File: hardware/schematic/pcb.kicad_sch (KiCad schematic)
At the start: 10 parts, among them J1 L, J2 R, J3 IR, J4 R n20 motor, J5 L n20 motor, J6 OLED, J7 L DRIVE, J8 R DRIVE, SW1 SW_DPST_x2

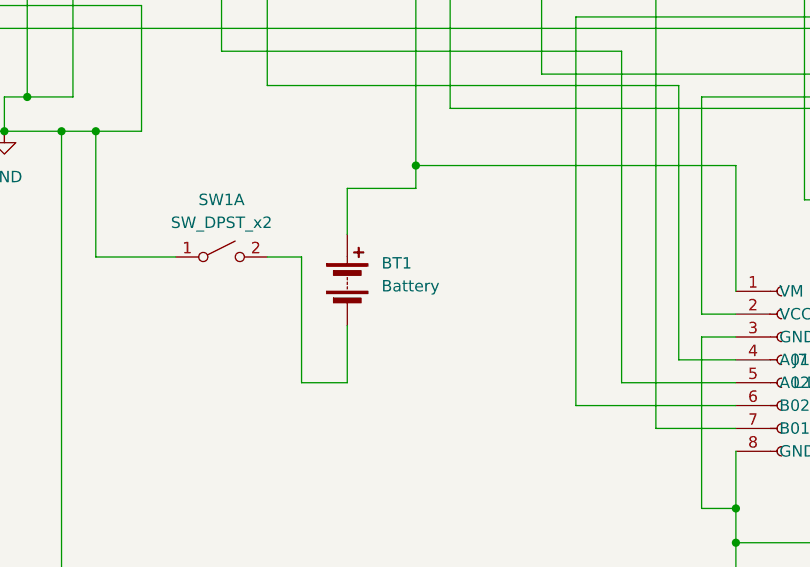
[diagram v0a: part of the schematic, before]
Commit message: Hardware: Minor schematic changes
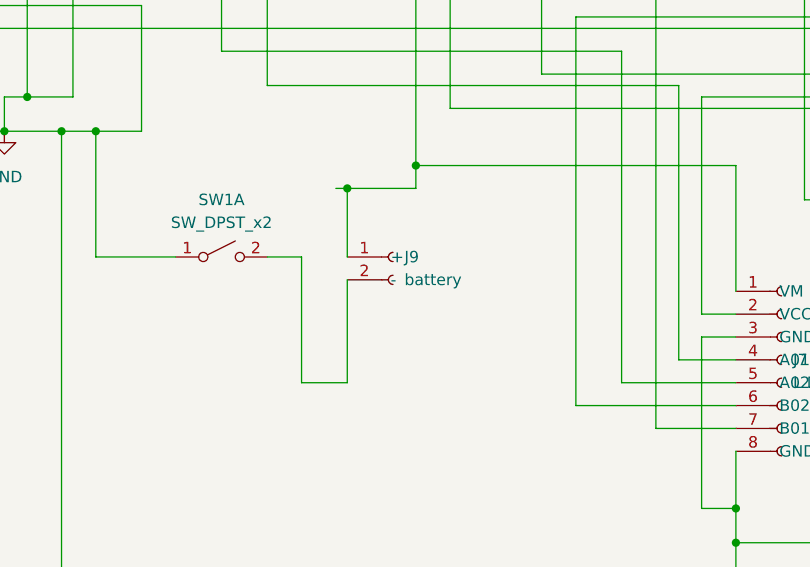
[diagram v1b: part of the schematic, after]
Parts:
- removed BT1: Battery, symbol Device:Battery
- added J9: battery, symbol Connector:Conn_01x02_Socket
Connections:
- net at SW1.2 (B): now also J9.2 (-)
- net at J1.15 (VIN), J7.1 (VM): now also J9.1 (+)
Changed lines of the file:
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@@
+	)
+	(junction
+		(at 81.28 139.7)
+		(diameter 0)
+		(color 0 0 0 0)
 	)
 	(junction
@@
 	(wire
 		(pts
+			(xy 81.28 149.86) (xy 81.28 161.29)
+		)
+		(stroke
+			(width 0)
+			(type default)
+		)
+	)
+	(wire
+		(pts
 			(xy 245.11 130.81) (xy 245.11 119.38)
 		)
@@
 	(wire
 		(pts
-			(xy 81.28 161.29) (xy 81.28 154.94)
-		)
-		(stroke
-			(width 0)
-			(type default)
-		)
-	)
-	(wire
-		(pts
 			(xy 72.39 80.01) (xy 72.39 128.27)
 		)
@@
 	(wire
 		(pts
+			(xy 80.01 139.7) (xy 81.28 139.7)
+		)
+		(stroke
+			(width 0)
+			(type default)
+		)
+	)
+	(wire
+		(pts
 			(xy 50.8 85.09) (xy 50.8 129.54)
 		)
@@
 	(wire
 		(pts
+			(xy 81.28 139.7) (xy 81.28 147.32)
+		)
+		(stroke
+			(width 0)
+			(type default)
+		)
+	)
+	(wire
+		(pts
 			(xy 167.64 35.56) (xy 167.64 38.1)
 		)
@@
 		(pts
 			(xy 111.76 49.53) (xy 111.76 80.01)
-		)
-		(stroke
-			(width 0)
-			(type default)
-		)
-	)
-	(wire
-		(pts
-			(xy 81.28 139.7) (xy 81.28 144.78)
 		)
 		(stroke
@@
 	)
 	(symbol
-		(lib_id "Device:Battery")
-		(at 81.28 149.86 0)
-		(unit 1)
-		(exclude_from_sim no)
-		(in_bom yes)
-		(on_board yes)
-		(dnp no)
-		(fields_autoplaced yes)
-		(property "Reference" "BT1"
-			(at 85.09 148.0184 0)
-			(effects
-				(font
-					(size 1.27 1.27)
-				)
-				(justify left)
-			)
-		)
-		(property "Value" "Battery"
-			(at 85.09 150.5584 0)
-			(effects
-				(font
-					(size 1.27 1.27)
-				)
-				(justify left)
-			)
-		)
-		(property "Footprint" ""
-			(at 81.28 148.336 90)
-			(effects
-				(font
-					(size 1.27 1.27)
-				)
-				(hide yes)
-			)
-		)
-		(property "Datasheet" "~"
-			(at 81.28 148.336 90)
-			(effects
-				(font
-					(size 1.27 1.27)
-				)
-				(hide yes)
-			)
-		)
-		(property "Description" "Multiple-cell battery"
-			(at 81.28 149.86 0)
-			(effects
-				(font
-					(size 1.27 1.27)
-				)
-				(hide yes)
-			)
-		)
-		(property "Sim.Device" "V"
-			(at 81.28 149.86 0)
-			(effects
-				(font
-					(size 1.27 1.27)
-				)
-				(hide yes)
-			)
-		)
-		(property "Sim.Type" "DC"
-			(at 81.28 149.86 0)
-			(effects
-				(font
-					(size 1.27 1.27)
-				)
-				(hide yes)
-			)
-		)
-		(property "Sim.Pins" "1=+ 2=-"
-			(at 81.28 149.86 0)
-			(effects
-				(font
-					(size 1.27 1.27)
-				)
-				(hide yes)
-			)
-		)
-		(pin "2"
-		)
-		(pin "1"
-		)
-		(instances
-			(project ""
-				(path "/bf33ebff-7199-46c5-b9b5-ecab4d26825a"
-					(reference "BT1")
-					(unit 1)
-				)
-			)
-		)
-	)
-	(symbol
 		(lib_id "Connector:Conn_01x06_Socket")
 		(at 191.77 87.63 0)
@@
 					(unit 1)
 				)
+			)
+		)
+	)
+	(symbol
+		(lib_id "Connector:Conn_01x02_Socket")
+		(at 86.36 147.32 0)
+		(unit 1)
+		(exclude_from_sim no)
+		(in_bom yes)
+		(on_board yes)
+		(dnp no)
+		(property "Reference" "J9"
+			(at 87.63 147.3199 0)
+			(effects
+				(font
+					(size 1.27 1.27)
+				)
+				(justify left)
+			)
+		)
+		(property "Value" "battery"
+			(at 87.63 149.8599 0)
+			(effects
+				(font
+					(size 1.27 1.27)
+				)
+				(justify left)
+			)
+		)
+		(property "Footprint" ""
+			(at 86.36 147.32 0)
+			(effects
+				(font
+					(size 1.27 1.27)
+				)
+				(hide yes)
+			)
+		)
+		(property "Datasheet" "~"
+			(at 86.36 147.32 0)
+			(effects
+				(font
+					(size 1.27 1.27)
+				)
+				(hide yes)
+			)
+		)
+		(property "Description" "Generic connector, single row, 01x02, script generated"
+			(at 86.36 147.32 0)
+			(effects
+				(font
+					(size 1.27 1.27)
+				)
+				(hide yes)
+			)
+		)
+		(pin "1"
+		)
+		(pin "2"
+		)
+		(instances
+			(project ""
+				(path "/bf33ebff-7199-46c5-b9b5-ecab4d26825a"
+					(reference "J9")
+					(unit 1)
+				)

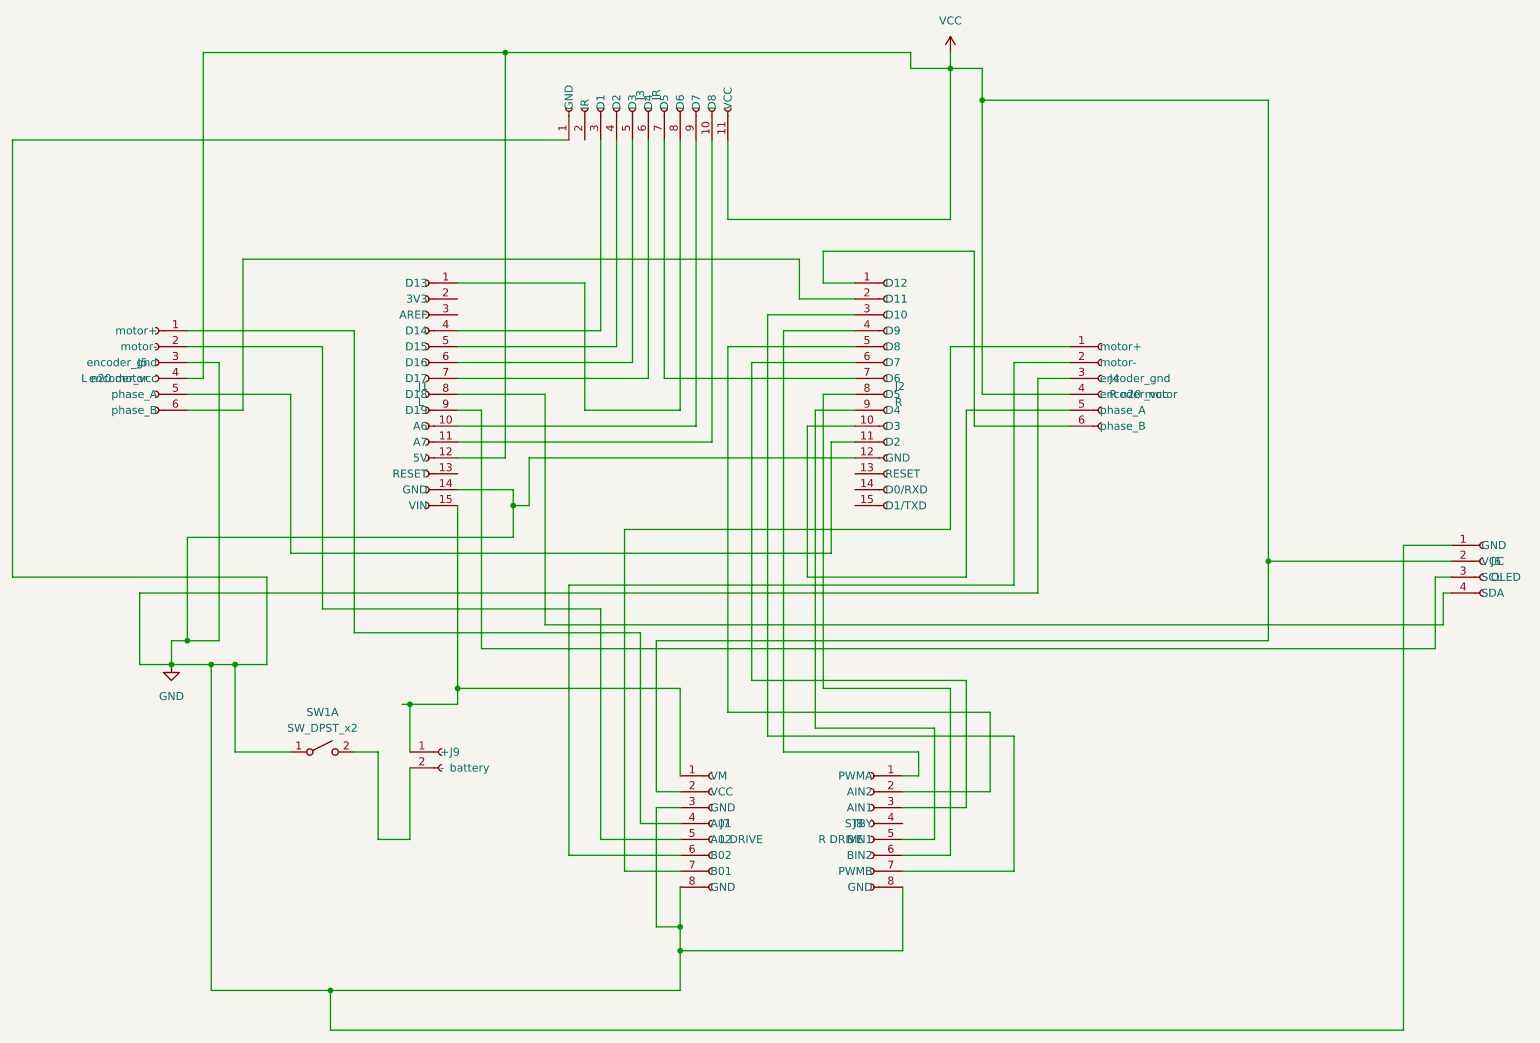
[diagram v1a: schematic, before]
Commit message: Hardware: Changed schematic according to new pin mapping
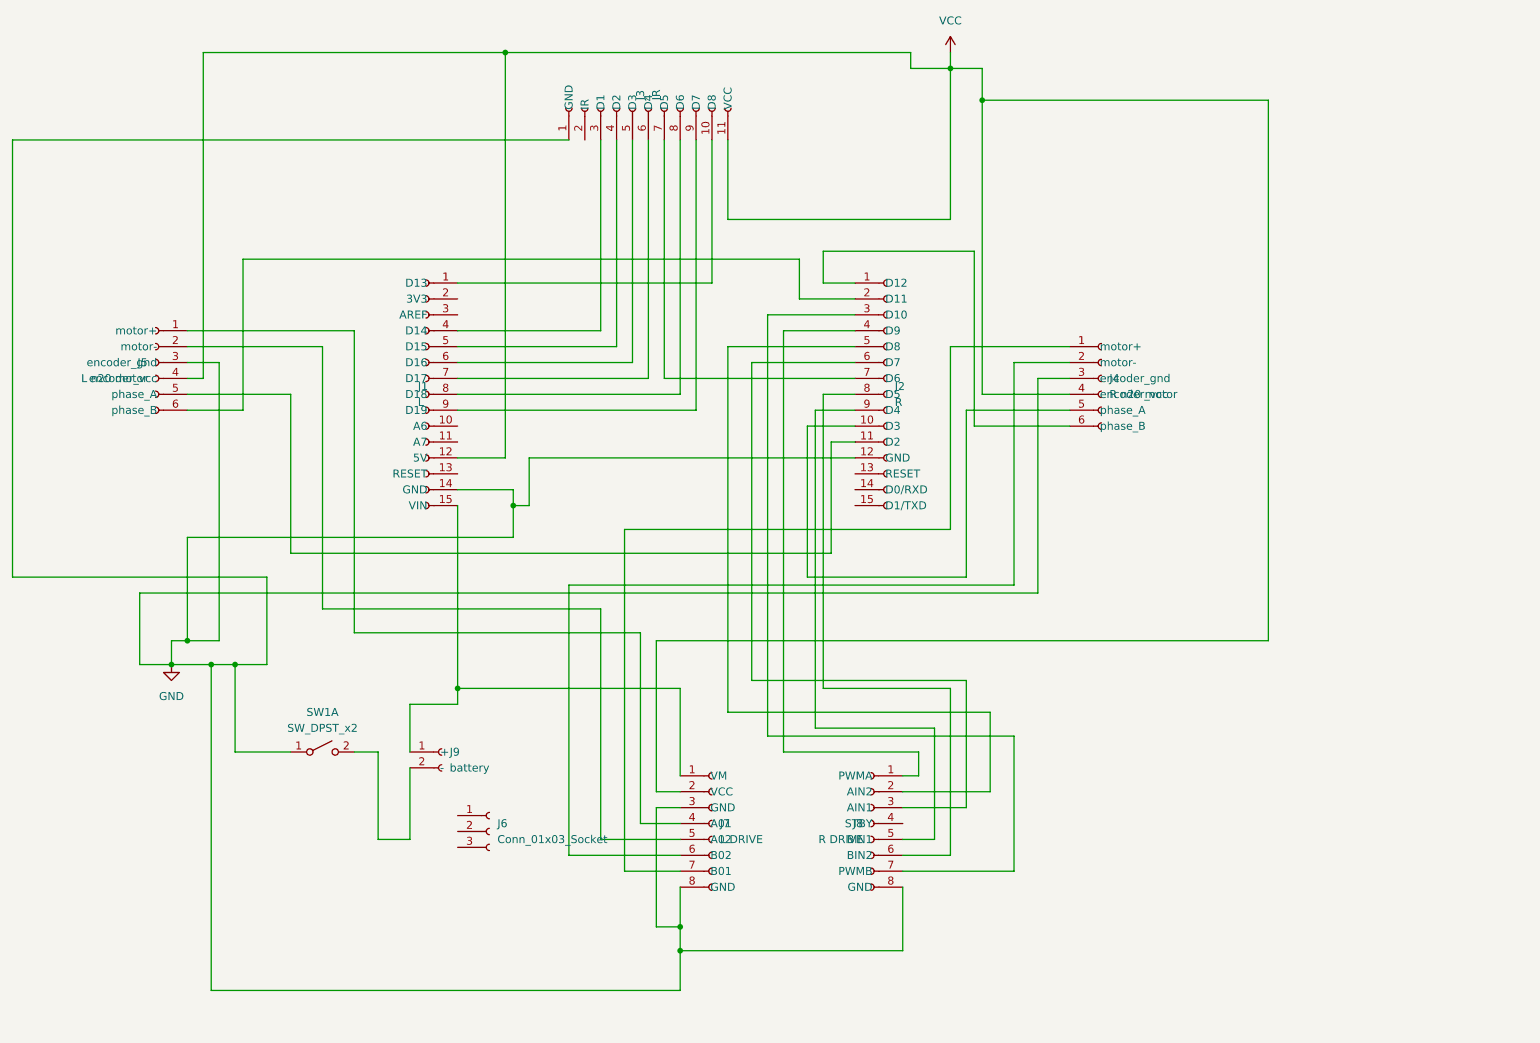
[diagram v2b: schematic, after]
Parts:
- removed J6: OLED, symbol Connector:Conn_01x04_Socket
- added J6: Conn_01x03_Socket, symbol Connector:Conn_01x03_Socket
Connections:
- net at J1.1 (D13): now also J3.10 (D8); no longer J3.8 (D6)
- net at J1.10 (A6): no longer J3.9 (D7)
- net at J1.11 (A7): no longer J3.10 (D8)
- net at J1.8 (D18): now also J3.8 (D6)
- net at J1.9 (D19): now also J3.9 (D7)
